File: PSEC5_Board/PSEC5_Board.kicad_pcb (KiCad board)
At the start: 4 copper layers, 76.2 x 76.2 mm, 187 parts, among them IC1 LTC6409IUDB#TRMPBF, IC2 LTC6409IUDB#TRMPBF, IC3 LTC6409IUDB#TRMPBF, IC4 LTC6409IUDB#TRMPBF, IC5 LTC6409IUDB#TRMPBF, IC6 LTC6409IUDB#TRMPBF, IC7 LTC6409IUDB#TRMPBF, IC8 LTC6409IUDB#TRMPBF, J1 QTH-040-01-X-D-DP-A, J11 Conn_Coaxial, J2 Conn_Coaxial, J3 Conn_Coaxial, J4 Conn_Coaxial, J5 Conn_Coaxial, J6 Conn_Coaxial, J7 Conn_Coaxial, J8 Conn_Coaxial, J9 QTH-040-01-X-D-DP-A, U1 MCP1700T-1802E_TT, U3 DAC8411IDCKT, U5 MC100LVEL, U6 OPA607QDBVRQ1, U7 AD4008BCPZ-RL7, Y1 ASE2-40.000MHZ-ET

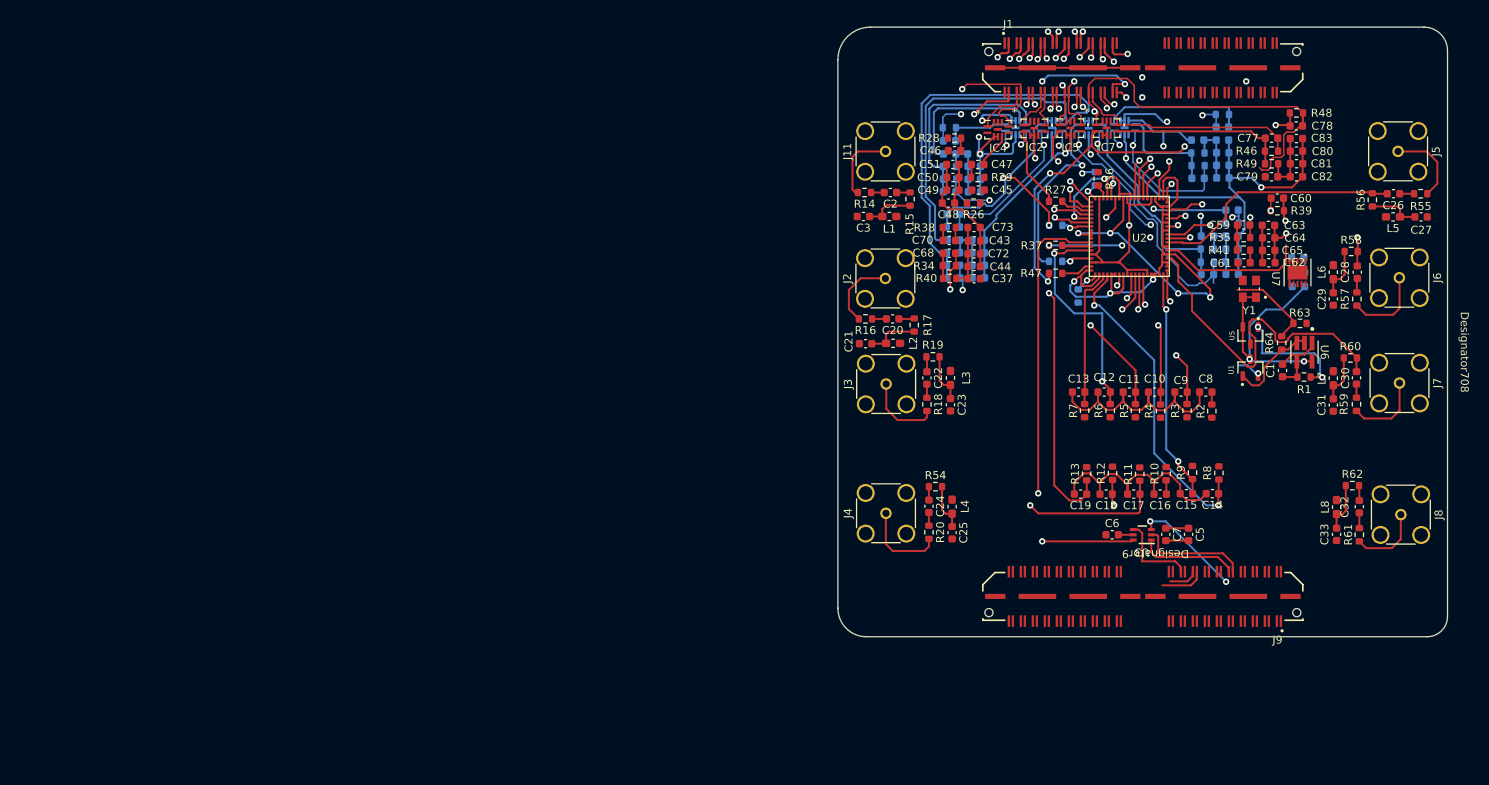
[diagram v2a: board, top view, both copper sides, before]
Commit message: DUT Layout finish 0.9
Still missing a ground plane, all other nets are connected.

Minor issue: Certain global labels are not being recognized: PSEC5_CLK_OUT
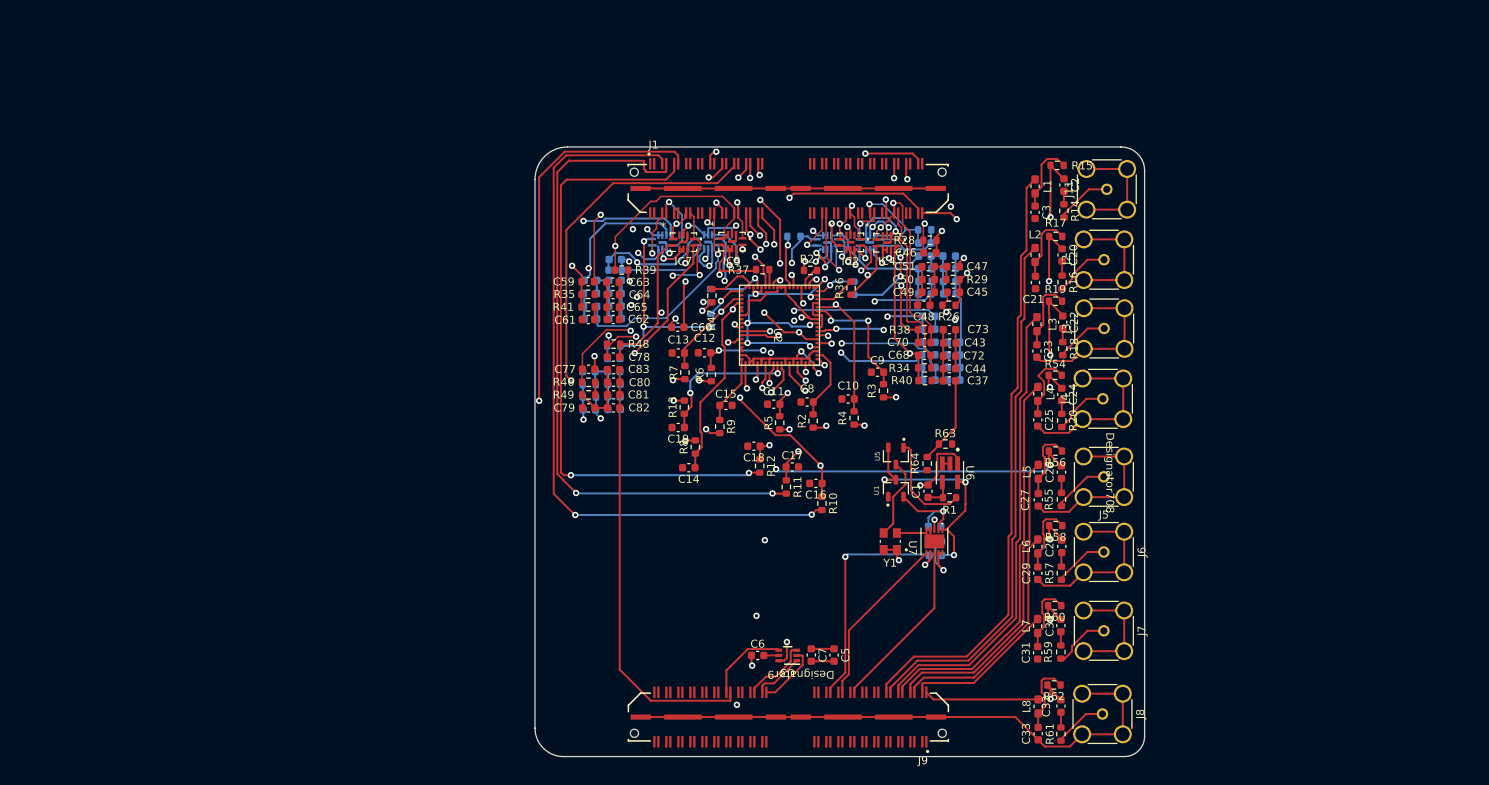
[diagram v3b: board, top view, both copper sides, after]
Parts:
- moved C78 90.1 mm to (124.7, 70.1)
- moved C82 90.1 mm to (124.7, 76.4)
- moved C83 90.1 mm to (124.7, 71.7)
- moved R48 90.1 mm to (124.7, 68.5)
- moved C77 90.1 mm to (121.6, 71.6)
- moved C79 90.1 mm to (121.6, 76.4)
- moved C80 90.1 mm to (124.8, 73.2)
- moved C81 90.1 mm to (124.8, 74.8)
- moved R46 90.1 mm to (121.6, 73.2)
- moved R49 90.1 mm to (121.7, 74.8)
- moved R39 82.3 mm to (125.8, 59.2)
- moved C62 82.3 mm to (124.7, 65.4)
- moved C61 82.3 mm to (121.6, 65.4)
- moved C63 82.3 mm to (124.7, 60.7)
- moved C64 82.3 mm to (124.7, 62.3)
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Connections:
- J1 pad 03: ReadClk -> unconnected-(J1-Pad03)
- J1 pad 04: POCI -> unconnected-(J1-Pad04)
- J1 pad 05: unconnected-(J1-Pad05) -> READBIAS1
- J1 pad 06: ADC1_Out+ -> ADC8_Out+
- J1 pad 07: rst -> READBIAS2
- J1 pad 08: ADC1_Out- -> ADC8_Out-
- J1 pad 09: SPIclk -> WBUFBIAS
- J1 pad 10: ADC2_Out+ -> unconnected-(J1-Pad10)
- J1 pad 11: PICO -> DISCBIAS
- J1 pad 12: ADC2_Out+ -> unconnected-(J1-Pad12)
- J1 pad 13: READBIAS1 -> unconnected-(J1-Pad13)
- J1 pad 14: ADC3_Out+ -> ADC7_Out+
- J1 pad 15: READBIAS2 -> unconnected-(J1-Pad15)
- J1 pad 16: ADC3_Out- -> ADC7_Out-
- J1 pad 17: WBUFBIAS -> unconnected-(J1-Pad17)
- J1 pad 18: ADC4_Out+ -> unconnected-(J1-Pad18)
- J1 pad 19: DISCBIAS -> unconnected-(J1-Pad19)
- J1 pad 20: ADC4_Out- -> unconnected-(J1-Pad20)
- J1 pad 21: Disc_Thresh1 -> Disc_Thresh8
- J1 pad 22: ADC5_Out+ -> ADC6_Out+
- J1 pad 23: Disc_Thresh2 -> unconnected-(J1-Pad23)
- J1 pad 24: ADC5_Out- -> ADC6_Out-
- J1 pad 25: Disc_Thresh3 -> Disc_Thresh7
- J1 pad 26: ADC6_Out+ -> TRIGGERIN
- J1 pad 27: Disc_Thresh4 -> unconnected-(J1-Pad27)
- J1 pad 28: ADC6_Out- -> unconnected-(J1-Pad28)
- J1 pad 29: Disc_Thresh5 -> Disc_Thresh6
- J1 pad 30: ADC7_Out+ -> ADC5_Out+
- J1 pad 31: Disc_Thresh6 -> unconnected-(J1-Pad31)
- J1 pad 32: ADC7_Out- -> ADC5_Out-
- J1 pad 33: Disc_Thresh7 -> Disc_Thresh5
- J1 pad 34: ADC8_Out+ -> rst
- J1 pad 35: Disc_Thresh8 -> PSEC5_CLK_OUT
- J1 pad 36: ADC8_Out- -> SPIclk
- J1 pad 37: TRIGGERIN -> Disc_Thresh4
- J1 pad 38: TRIGGEROUT -> ReadClk
- J1 pad 40: PSEC5_CLK_OUT -> TRIGGEROUT
- J1 pad 46: unconnected-(J1-Pad46) -> ADC4_Out+
- J1 pad 48: unconnected-(J1-Pad48) -> ADC4_Out-
- J1 pad 54: unconnected-(J1-Pad54) -> ADC3_Out+
- J1 pad 56: unconnected-(J1-Pad56) -> ADC3_Out-
- J1 pad 62: unconnected-(J1-Pad62) -> ADC2_Out+
- J1 pad 64: unconnected-(J1-Pad64) -> ADC2_Out-
- J1 pad 68: unconnected-(J1-Pad68) -> PICO
- J1 pad 69: unconnected-(J1-Pad69) -> Disc_Thresh3
- J1 pad 70: unconnected-(J1-Pad70) -> ADC1_Out+
- J1 pad 72: unconnected-(J1-Pad72) -> ADC1_Out-
- J1 pad 73: unconnected-(J1-Pad73) -> Disc_Thresh2
- J1 pad 77: unconnected-(J1-Pad77) -> Disc_Thresh1
- J1 pad 80: unconnected-(J1-Pad80) -> POCI
- J1 pad G5: unconnected-(J1B-GND2-PadG5) -> GND
- J1 pad G6: unconnected-(J1B-GND2__1-PadG6) -> GND
- J1 pad G7: unconnected-(J1B-GND2__2-PadG7) -> GND
- J1 pad G8: unconnected-(J1B-GND2__3-PadG8) -> GND
- J9 pad 02: V_ped1 -> V_ped8
- J9 pad 04: V_ped2 -> V_ped7
- J9 pad 06: V_ped3 -> V_ped6
- J9 pad 08: V_ped4 -> V_ped5
- J9 pad 10: V_ped5 -> V_ped4
- J9 pad 12: V_ped6 -> V_ped3
- J9 pad 14: V_ped7 -> V_ped2
- J9 pad 16: V_ped8 -> V_ped1
- J9 pad 18: DAC_SCLK -> unconnected-(J9-Pad18)
- J9 pad 20: SYNC_N -> unconnected-(J9-Pad20)
- J9 pad 22: DAC_V_IN -> unconnected-(J9-Pad22)
- J9 pad 24: ADC_SCK -> unconnected-(J9-Pad24)
- J9 pad 26: ADC_SDO -> ADC_SCK
- J9 pad 28: ADC_CNV -> unconnected-(J9-Pad28)
- J9 pad 30: VDD -> ADC_CNV
- J9 pad 32: VDD18 -> unconnected-(J9-Pad32)
- J9 pad 34: VDD33 -> ADC_SDO
- J9 pad 36: VDD25 -> unconnected-(J9-Pad36)
- J9 pad 38: VDD50 -> unconnected-(J9-Pad38)
- J9 pad 42: unconnected-(J9-Pad42) -> DAC_SCLK
- J9 pad 44: unconnected-(J9-Pad44) -> SYNC_N
- J9 pad 46: unconnected-(J9-Pad46) -> DAC_V_IN
- J9 pad 50: unconnected-(J9-Pad50) -> VDD
- J9 pad 52: unconnected-(J9-Pad52) -> VDD18
- J9 pad 54: unconnected-(J9-Pad54) -> VDD33
- J9 pad 56: unconnected-(J9-Pad56) -> VDD25
- J9 pad 58: unconnected-(J9-Pad58) -> VDD50
- J9 pad G5: unconnected-(J9B-GND2-PadG5) -> GND
- J9 pad G6: unconnected-(J9B-GND2__1-PadG6) -> GND
- J9 pad G7: unconnected-(J9B-GND2__2-PadG7) -> GND
- J9 pad G8: unconnected-(J9B-GND2__3-PadG8) -> GND
- U2 pad 9: /Phase_detection/PSEC5_CLK_OUT -> PSEC5_CLK_OUT
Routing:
- net GND: track 211.6 -> 351.6 mm, vias 5 -> 6
- net READBIAS1: track 2.17 -> 90.6 mm, vias 1 -> 2
- net READBIAS2: track 2.03 -> 83.9 mm, vias 1 -> 2
- net /Pedestals/SIGNAL8: track 5.89 -> 87.3 mm, vias 1 -> 3
- net V_ped1: track 0.00 -> 75.7 mm
- net WBUFBIAS: track 1.67 -> 76.9 mm, vias 1 -> 2
- net V_ped2: track 0.00 -> 66.8 mm
- net DISCBIAS: track 1.53 -> 66.0 mm, vias 1 -> 2
- net V_ped3: track 0.00 -> 57.8 mm
- net Disc_Thresh6: track 1.90 -> 58.0 mm, vias 1 -> 2
- net /Pedestals/SIGNAL1: track 4.21 -> 56.2 mm, vias 1 -> 2
- net V_ped4: track 0.00 -> 49.1 mm
- net Disc_Thresh1: track 2.34 -> 49.7 mm, vias 1 -> 2
- net +2V5: track 43.2 -> 87.8 mm, vias 2 -> 8
- net Disc_Thresh8: track 2.80 -> 45.8 mm, vias 1 -> 2
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
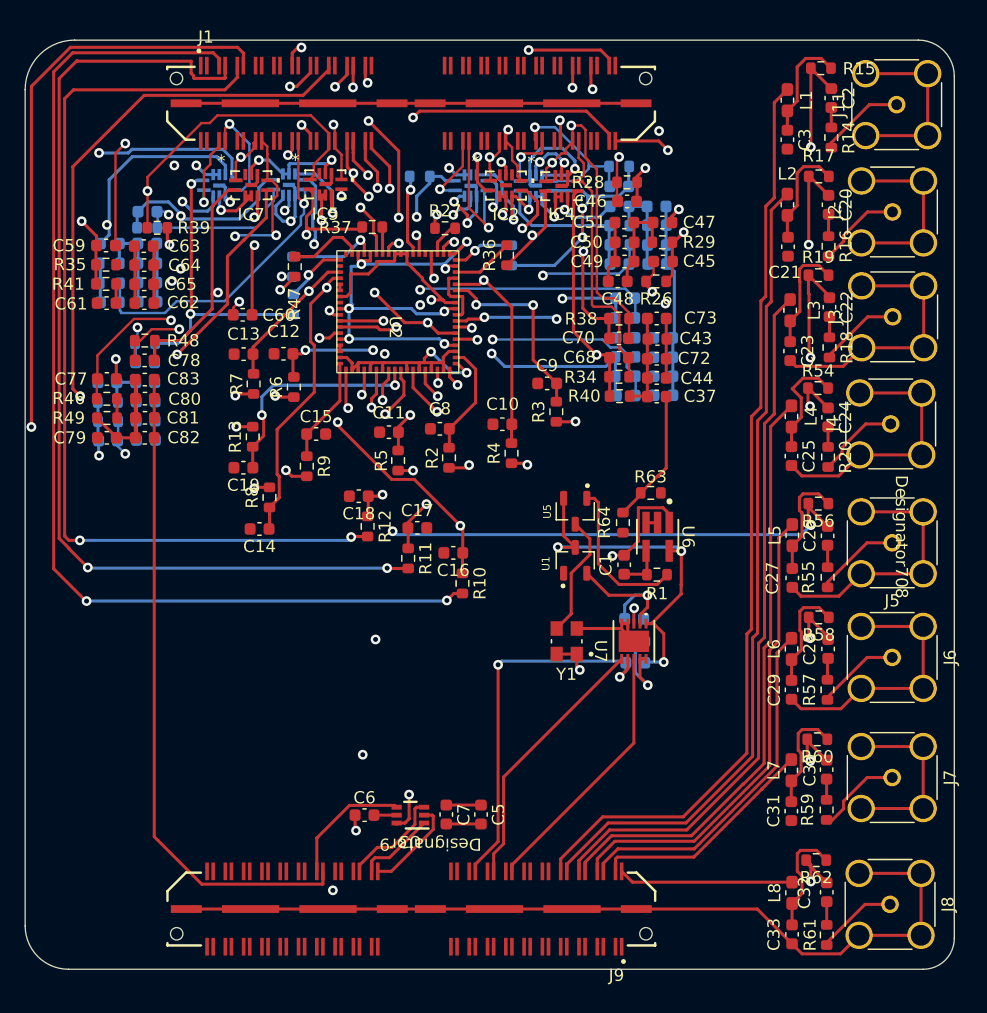
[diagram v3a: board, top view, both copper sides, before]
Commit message: DUT ERC changes #1
Fixed some thermal issues, overlapping courtyards.
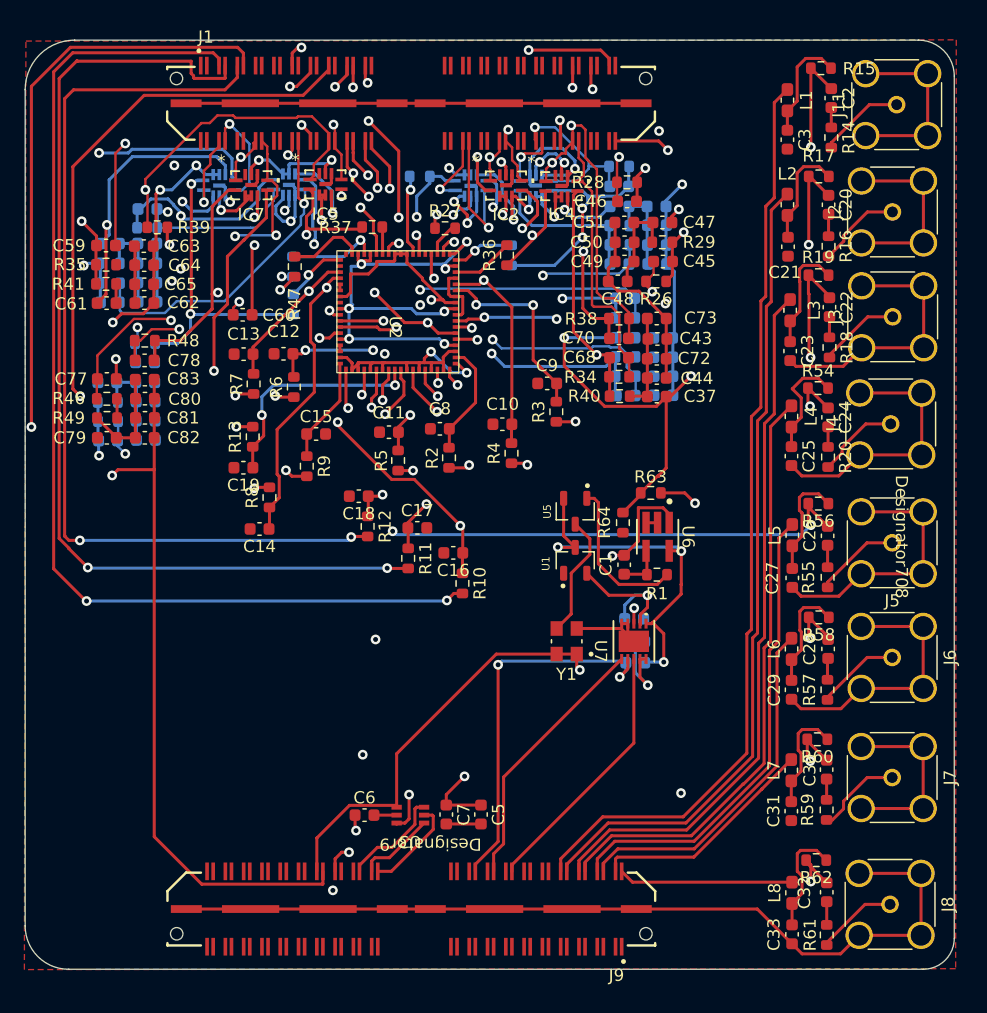
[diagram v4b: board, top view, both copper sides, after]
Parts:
- moved C67 0.22 mm to (125.0, 57.7)
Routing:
- net VDD18: track 0.00 -> 59.0 mm, vias 0 -> 3
- net VDD33: track 167.5 -> 221.7 mm, vias 13 -> 17
- net V_OCM: track 105.1 -> 145.4 mm, vias 7 -> 9
- net +1V2: track 44.3 -> 81.1 mm, vias 3 -> 4
- net Net-(IC6--IN): track 9.30 -> 30.3 mm, vias 1 -> 2
- net VDD25: track 50.4 -> 71.3 mm
- net unconnected-(J1-Pad78): track 17.7 -> 0.58 mm, vias 1 -> 0
- net Net-(IC7--IN): track 25.0 -> 28.3 mm
- net GND: track 351.6 -> 352.8 mm
- added copper zone on F.Cu, net GND

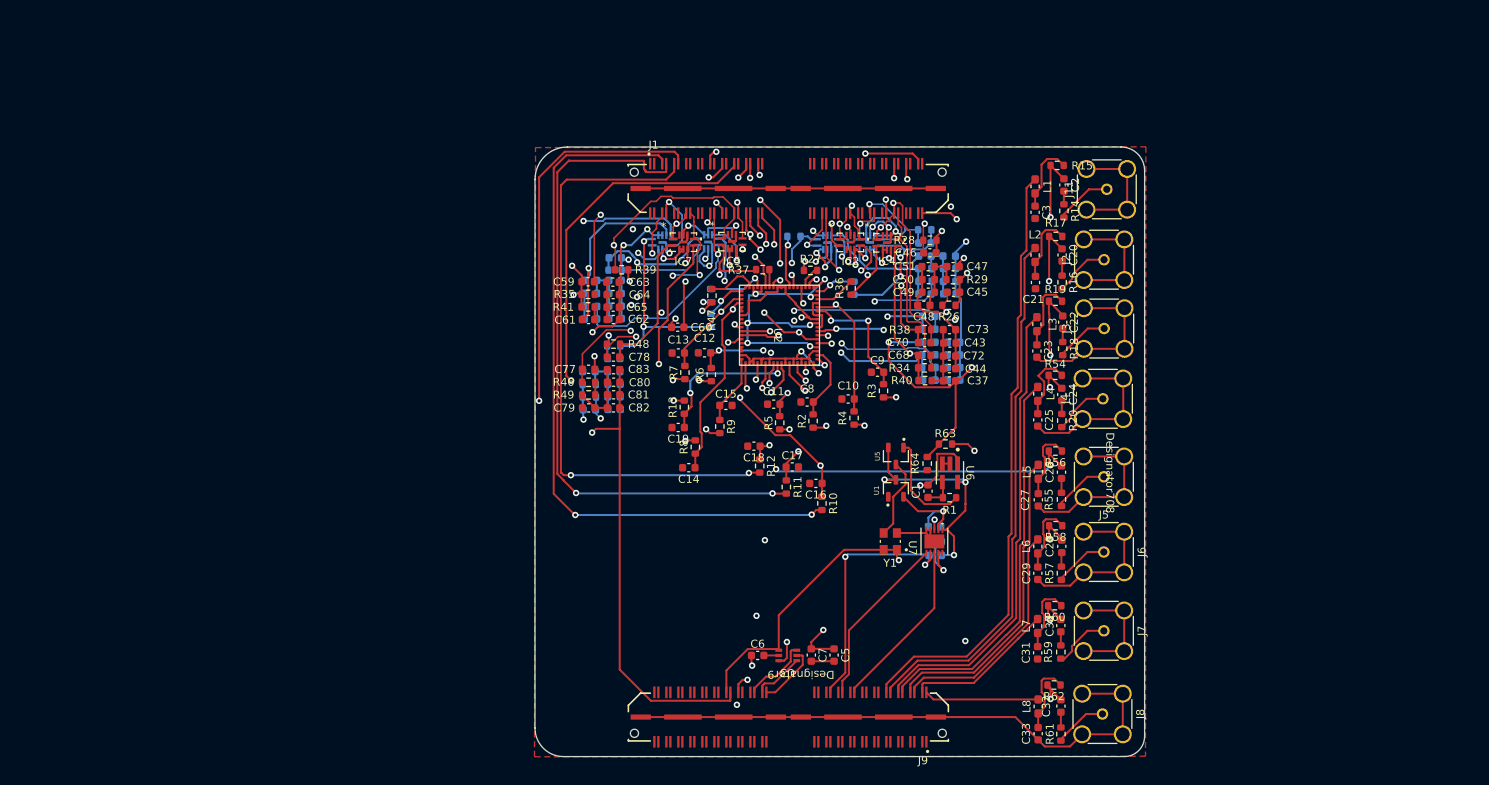
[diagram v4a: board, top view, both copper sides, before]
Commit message: changes to layout
Made board 6 layers and starting to re-route tracks on layout design
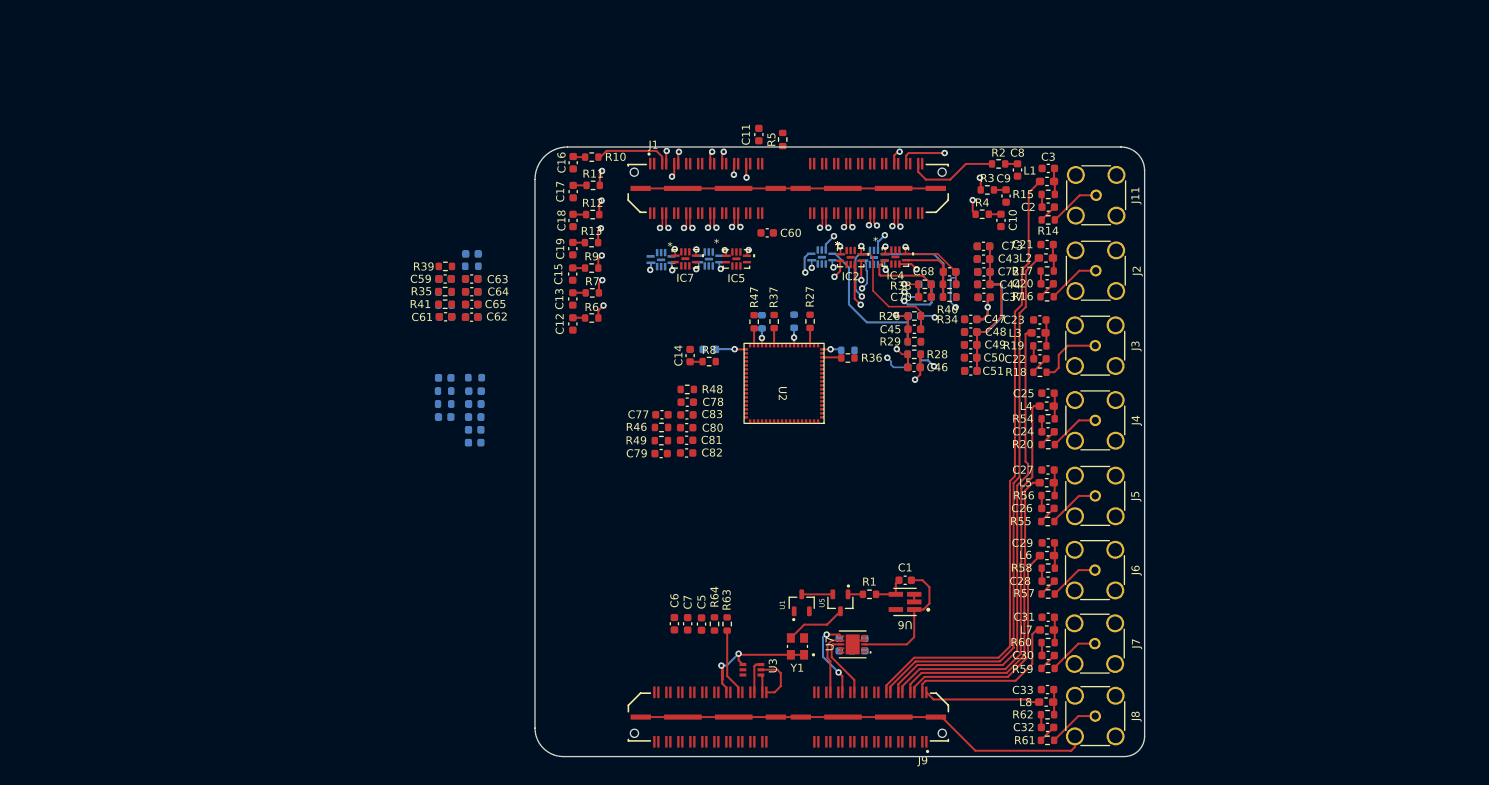
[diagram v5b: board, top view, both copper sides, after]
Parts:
- moved R10 52.0 mm to (122.0, 45.1), turned to 0 degrees
- moved C16 50.3 mm to (119.7, 45.8), turned to -90 degrees
- moved R11 44.8 mm to (122.2, 48.6), turned to 0 degrees
- moved C17 44.0 mm to (119.7, 49.4), turned to -90 degrees
- moved R2 39.6 mm to (172.9, 45.9), turned to 180 degrees
- moved C8 39.1 mm to (175.2, 46.7), turned to -90 degrees
- moved R12 37.7 mm to (122.2, 52.3), turned to 0 degrees
- moved C18 36.2 mm to (119.7, 53.0), turned to -90 degrees
- moved R5 35.4 mm to (145.9, 42.9)
- moved R63 35.4 mm to (139.0, 103.5), turned to 90 degrees
- moved C11 33.8 mm to (142.9, 42.3), turned to -90 degrees
- moved R64 33.3 mm to (137.4, 103.4)
- moved R4 30.1 mm to (170.8, 52.2), turned to 180 degrees
- moved C10 29.4 mm to (173.2, 53.0), turned to -90 degrees
- moved R3 28.3 mm to (171.5, 49.2), turned to 180 degrees
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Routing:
- net GND: track 352.8 -> 97.6 mm, vias 6 -> 0
- net VDD33: track 221.7 -> 37.9 mm, vias 17 -> 0
- net V_OCM: track 145.4 -> 45.6 mm, vias 9 -> 5
- net +2V5: track 87.8 -> 0.00 mm, vias 8 -> 0
- net /Pedestals/SIGNAL8: track 87.3 -> 1.61 mm, vias 3 -> 0
- net READBIAS1: track 90.6 -> 9.48 mm, vias 2 -> 0
- net +1V2: track 81.1 -> 0.00 mm, vias 4 -> 0
- net READBIAS2: track 83.9 -> 12.7 mm
- net /Pedestals/SIGNAL7: track 72.9 -> 1.63 mm, vias 3 -> 0
- net WBUFBIAS: track 76.9 -> 14.8 mm
- net /Pedestals/SIGNAL6: track 62.3 -> 1.64 mm, vias 3 -> 0
- net /Pedestals/SIGNAL1: track 56.2 -> 1.61 mm, vias 2 -> 0
- net /Pedestals/SIGNAL5: track 53.0 -> 1.61 mm, vias 3 -> 0
- net VDD18: track 59.0 -> 8.30 mm, vias 3 -> 0
- net DAC_V_OUT: track 50.6 -> 0.00 mm, vias 2 -> 0
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- removed copper zone on F.Cu, net GND
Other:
- copper layers 4 -> 6
